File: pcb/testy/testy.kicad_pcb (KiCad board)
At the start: 2 copper layers, 155.3 x 101.9 mm, 38 parts, among them SW0:0 SW_Push, SW0:1 SW_Push, SW0:2 SW_Push, SW1:0 SW_Push, SW1:1 SW_Push, SW1:2 SW_Push, U1 ProMicro

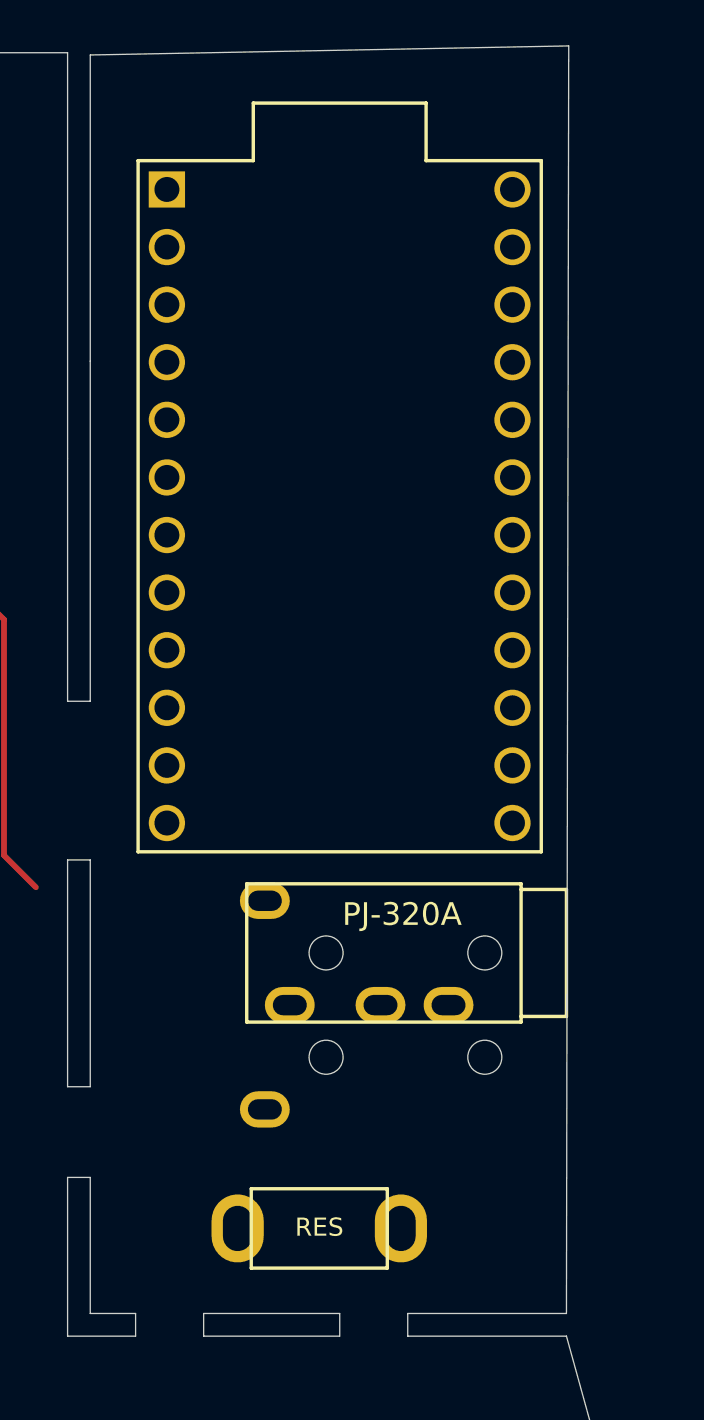
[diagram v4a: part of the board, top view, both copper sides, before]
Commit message: chore: add some 4 pin reset switches, played with new footprints
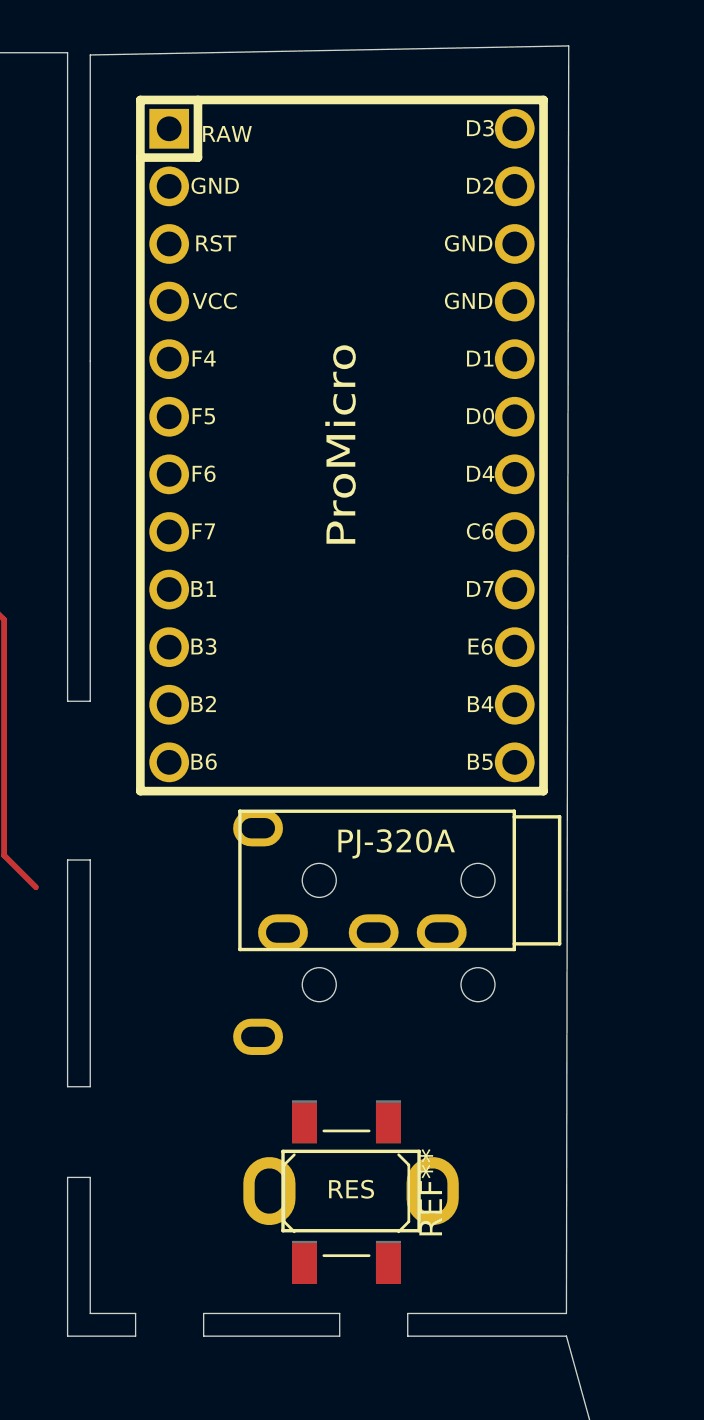
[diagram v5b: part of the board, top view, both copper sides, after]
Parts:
- added REF**: SW_SPST_TL3342, footprints:SW_TACT_ALPS_SKQGABE010, B.Cu at (188.3, 71.6)
- added REF**: SW_SPST_TL3342, footprints:SW_TACT_ALPS_SKQGABE010, F.Cu at (188.3, 71.7)
- U1: footprint promicro:ProMicro -> footprints:Pro_Micro_ergotravel
- moved U1 4.20 mm to (188.1, 37.2), turned to 0 degrees
- moved TRRS1 3.21 mm to (195.7, 60.2)
- moved SW-reset1 2.16 mm to (188.5, 69.8)
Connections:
- U1 pad 1: Net-(U1-Pad1) -> (no net)
- U1 pad 10: Col5 -> (no net)
- U1 pad 11: Col6 -> (no net)
- U1 pad 12: LED2 -> (no net)
- U1 pad 13: Net-(U1-Pad13) -> (no net)
- U1 pad 14: data -> (no net)
- U1 pad 15: GND -> (no net)
- U1 pad 16: GND -> (no net)
- U1 pad 17: Net-(U1-Pad17) -> (no net)
- U1 pad 18: LED0 -> (no net)
- U1 pad 19: Row0 -> (no net)
- U1 pad 2: GND -> (no net)
- U1 pad 20: Row1 -> (no net)
- U1 pad 21: Row2 -> (no net)
- U1 pad 22: Row3 -> (no net)
- U1 pad 23: Row4 -> (no net)
- U1 pad 24: LED1 -> (no net)
- U1 pad 3: Reset -> (no net)
- U1 pad 4: VCC -> (no net)
- U1 pad 5: Col0 -> (no net)
- U1 pad 6: Col1 -> (no net)
- U1 pad 7: Col2 -> (no net)
- U1 pad 8: Col3 -> (no net)
- U1 pad 9: Col4 -> (no net)
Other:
- board text added: "<-- wire all these switches together"

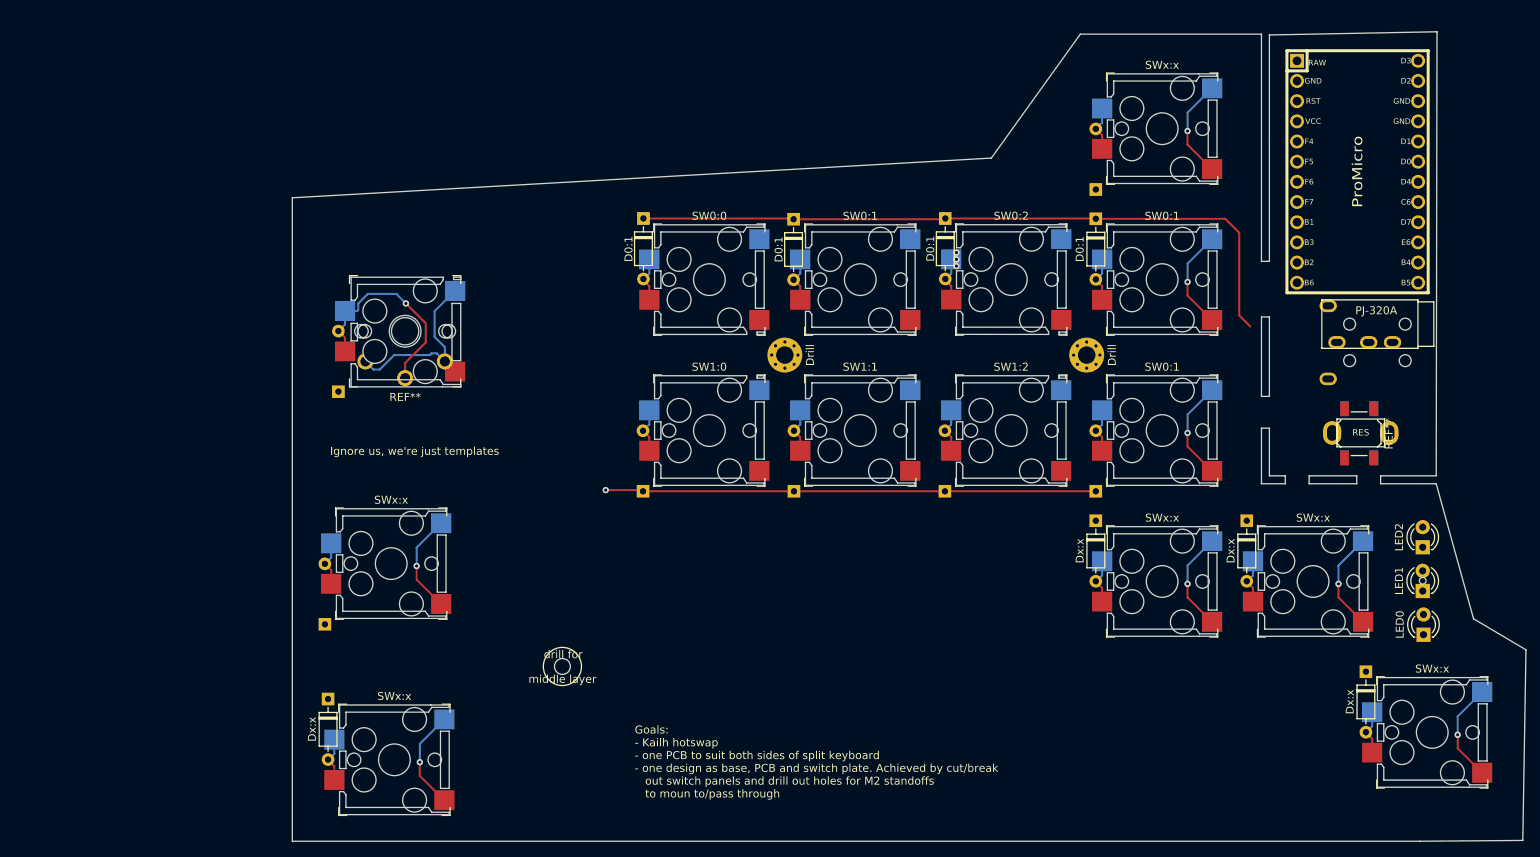
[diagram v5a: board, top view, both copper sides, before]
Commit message: feat: remove footprint with solder on for fullsize MX switches, that wasn't ever going to work; fix existing combo footprint to add clearance for choc switches, start the col stagger layout
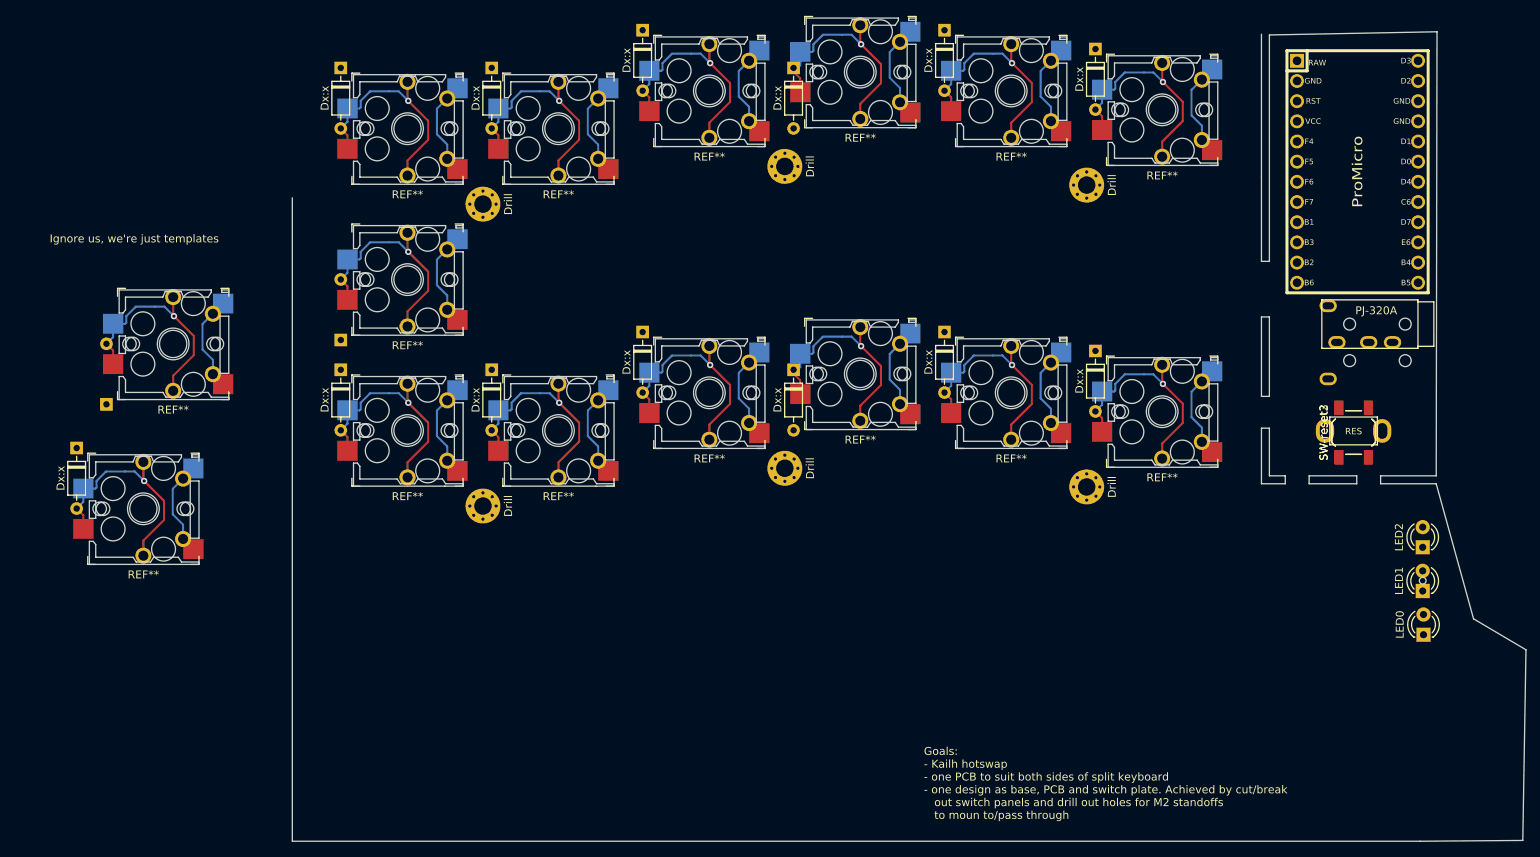
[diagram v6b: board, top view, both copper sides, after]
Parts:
- removed D0:1 (x8): 1N4148, Diode_THT:D_DO-35_SOD27_P7.62mm_Horizontal
- removed the Drill at (154.0, 61.8)
- removed the Dx:x at (155.2, 41.0)
- removed the Dx:x at (189.2, 101.7)
- removed the Dx:x at (174.2, 82.7)
- removed the Dx:x at (155.2, 82.7)
- removed the Dx:x at (58.5, 105.1)
- removed the Dx:x at (58.1, 95.7)
- removed the REF** at (188.3, 71.6)
- removed the REF** at (188.3, 71.7)
- removed SW0:0, SW0:1 (x3), SW0:2, SW1:0, SW1:1, SW1:2, SWx:x (x6): SW_Push, footprints:Kailh_socket_reversible
- added Drill: MountingHole_2.2mm_M2_Pad_Via, MountingHole:MountingHole_2.2mm_M2_Pad_Via, F.Cu at (116.0, 76.0)
- added Drill: MountingHole_2.2mm_M2_Pad_Via, MountingHole:MountingHole_2.2mm_M2_Pad_Via, F.Cu at (78.0, 80.8)
- added Drill: MountingHole_2.2mm_M2_Pad_Via, MountingHole:MountingHole_2.2mm_M2_Pad_Via, F.Cu at (154.0, 78.4)
- added Drill: MountingHole_2.2mm_M2_Pad_Via, MountingHole:MountingHole_2.2mm_M2_Pad_Via, F.Cu at (154.0, 40.4)
- added Drill: MountingHole_2.2mm_M2_Pad_Via, MountingHole:MountingHole_2.2mm_M2_Pad_Via, F.Cu at (116.0, 38.0)
- added Dx:x: 1N4148, Diode_THT:D_DO-35_SOD27_P7.62mm_Horizontal, F.Cu at (155.1, 61.3)
- added Dx:x: 1N4148, Diode_THT:D_DO-35_SOD27_P7.62mm_Horizontal, F.Cu at (117.1, 25.6)
- added Dx:x: 1N4148, Diode_THT:D_DO-35_SOD27_P7.62mm_Horizontal, F.Cu at (136.1, 20.9)
- added Dx:x: 1N4148, Diode_THT:D_DO-35_SOD27_P7.62mm_Horizontal, F.Cu at (155.1, 23.3)
- added Dx:x: 1N4148, Diode_THT:D_DO-35_SOD27_P7.62mm_Horizontal, F.Cu at (98.1, 20.9)
- added Dx:x: 1N4148, Diode_THT:D_DO-35_SOD27_P7.62mm_Horizontal, F.Cu at (26.9, 73.5)
- added Dx:x: 1N4148, Diode_THT:D_DO-35_SOD27_P7.62mm_Horizontal, F.Cu at (79.1, 63.6)
- added Dx:x: 1N4148, Diode_THT:D_DO-35_SOD27_P7.62mm_Horizontal, F.Cu at (117.1, 63.6)
- added Dx:x: 1N4148, Diode_THT:D_DO-35_SOD27_P7.62mm_Horizontal, F.Cu at (136.1, 58.9)
- added Dx:x: 1N4148, Diode_THT:D_DO-35_SOD27_P7.62mm_Horizontal, F.Cu at (60.1, 63.6)
- added Dx:x: 1N4148, Diode_THT:D_DO-35_SOD27_P7.62mm_Horizontal, F.Cu at (98.1, 58.9)
- added Dx:x: 1N4148, Diode_THT:D_DO-35_SOD27_P7.62mm_Horizontal, B.Cu at (60.1, 59.9)
- added Dx:x: 1N4148, Diode_THT:D_DO-35_SOD27_P7.62mm_Horizontal, F.Cu at (60.1, 25.6)
- added Dx:x: 1N4148, Diode_THT:D_DO-35_SOD27_P7.62mm_Horizontal, F.Cu at (79.1, 25.6)
- added REF**: PG1511_socket, footprints:kailh-socket-and-choc-solder-reversible, F.Cu at (125.5, 64.2)
- added REF**: PG1511_socket, footprints:kailh-socket-and-choc-solder-reversible, F.Cu at (125.5, 26.2)
- added REF**: PG1511_socket, footprints:kailh-socket-and-choc-solder-reversible, F.Cu at (144.5, 28.6)
- added REF**: PG1511_socket, footprints:kailh-socket-and-choc-solder-reversible, F.Cu at (163.5, 30.9)
- added REF**: PG1511_socket, footprints:kailh-socket-and-choc-solder-reversible, F.Cu at (106.5, 28.6)
- added REF**: PG1511_socket, footprints:kailh-socket-and-choc-solder-reversible, F.Cu at (35.2, 81.2)
- added REF**: PG1511_socket, footprints:kailh-socket-and-choc-solder-reversible, F.Cu at (87.5, 71.3)
- added REF**: PG1511_socket, footprints:kailh-socket-and-choc-solder-reversible, F.Cu at (144.5, 66.5)
- added REF**: PG1511_socket, footprints:kailh-socket-and-choc-solder-reversible, F.Cu at (68.5, 71.3)
- added REF**: PG1511_socket, footprints:kailh-socket-and-choc-solder-reversible, F.Cu at (106.5, 66.5)
- added REF**: PG1511_socket, footprints:kailh-socket-and-choc-solder-reversible, F.Cu at (163.5, 68.9)
- added REF**: PG1511_socket, footprints:kailh-socket-and-choc-solder-reversible, F.Cu at (68.5, 52.3)
- added REF**: PG1511_socket, footprints:kailh-socket-and-choc-solder-reversible, F.Cu at (68.5, 33.3)
- added REF**: PG1511_socket, footprints:kailh-socket-and-choc-solder-reversible, F.Cu at (87.5, 33.3)
- added SW-reset2, SW-reset3: SW_Push, footprints:SW_TACT_ALPS_SKQGABE010, F.Cu at (187.6, 71.5)
- moved Drill 42.5 mm to (78.0, 42.8)
- moved REF** 29.2 mm to (39.0, 60.4)
- moved Dx:x 29.2 mm to (30.6, 68.0)
- moved SW-reset1 3.37 mm to (187.6, 73.1), turned to 0 degrees
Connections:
- U1 pad 1: (no net) -> Net-(U1-Pad1)
- U1 pad 10: (no net) -> Col5
- U1 pad 11: (no net) -> Col6
- U1 pad 12: (no net) -> LED2
- U1 pad 13: (no net) -> Net-(U1-Pad13)
- U1 pad 14: (no net) -> data
- U1 pad 15: (no net) -> GND
- U1 pad 16: (no net) -> GND
- U1 pad 17: (no net) -> Net-(U1-Pad17)
- U1 pad 18: (no net) -> LED0
- U1 pad 19: (no net) -> Row0
- U1 pad 2: (no net) -> GND
- U1 pad 20: (no net) -> Row1
- U1 pad 21: (no net) -> Row2
- U1 pad 22: (no net) -> Row3
- U1 pad 23: (no net) -> Row4
- U1 pad 24: (no net) -> LED1
- U1 pad 3: (no net) -> Reset
- U1 pad 4: (no net) -> VCC
- U1 pad 5: (no net) -> Col0
- U1 pad 6: (no net) -> Col1
- U1 pad 7: (no net) -> Col2
- U1 pad 8: (no net) -> Col3
- U1 pad 9: (no net) -> Col4
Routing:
- net (no net): track 161.6 -> 621.7 mm, vias 7 -> 15
- net Row0: track 150.0 -> 0.00 mm, vias 1 -> 0
- net Col1: track 25.5 -> 0.00 mm, vias 2 -> 0
- net Net-(D0:1-Pad2): track 17.2 -> 0.00 mm
- net Net-(D0:0-Pad2): track 5.73 -> 0.00 mm
- net Net-(D1:2-Pad2): track 5.73 -> 0.00 mm
- net Net-(D1:1-Pad2): track 5.73 -> 0.00 mm
- net Net-(D1:0-Pad2): track 5.73 -> 0.00 mm
- net Net-(D0:2-Pad2): track 5.73 -> 0.00 mm, vias 3 -> 0
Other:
- board size 155.3 x 101.9 mm -> 180.9 x 103.6 mm
- board text removed: "<-- wire all these switches together"
- board text removed: "FIXME will this via mouse bite trick work?"
- board text removed: "drill for"
- board text removed: "middle layer"
